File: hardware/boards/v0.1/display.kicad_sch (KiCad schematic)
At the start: 10 parts, among them U26 ER-TFT028A-4, U37 ER-TPC028-4.1

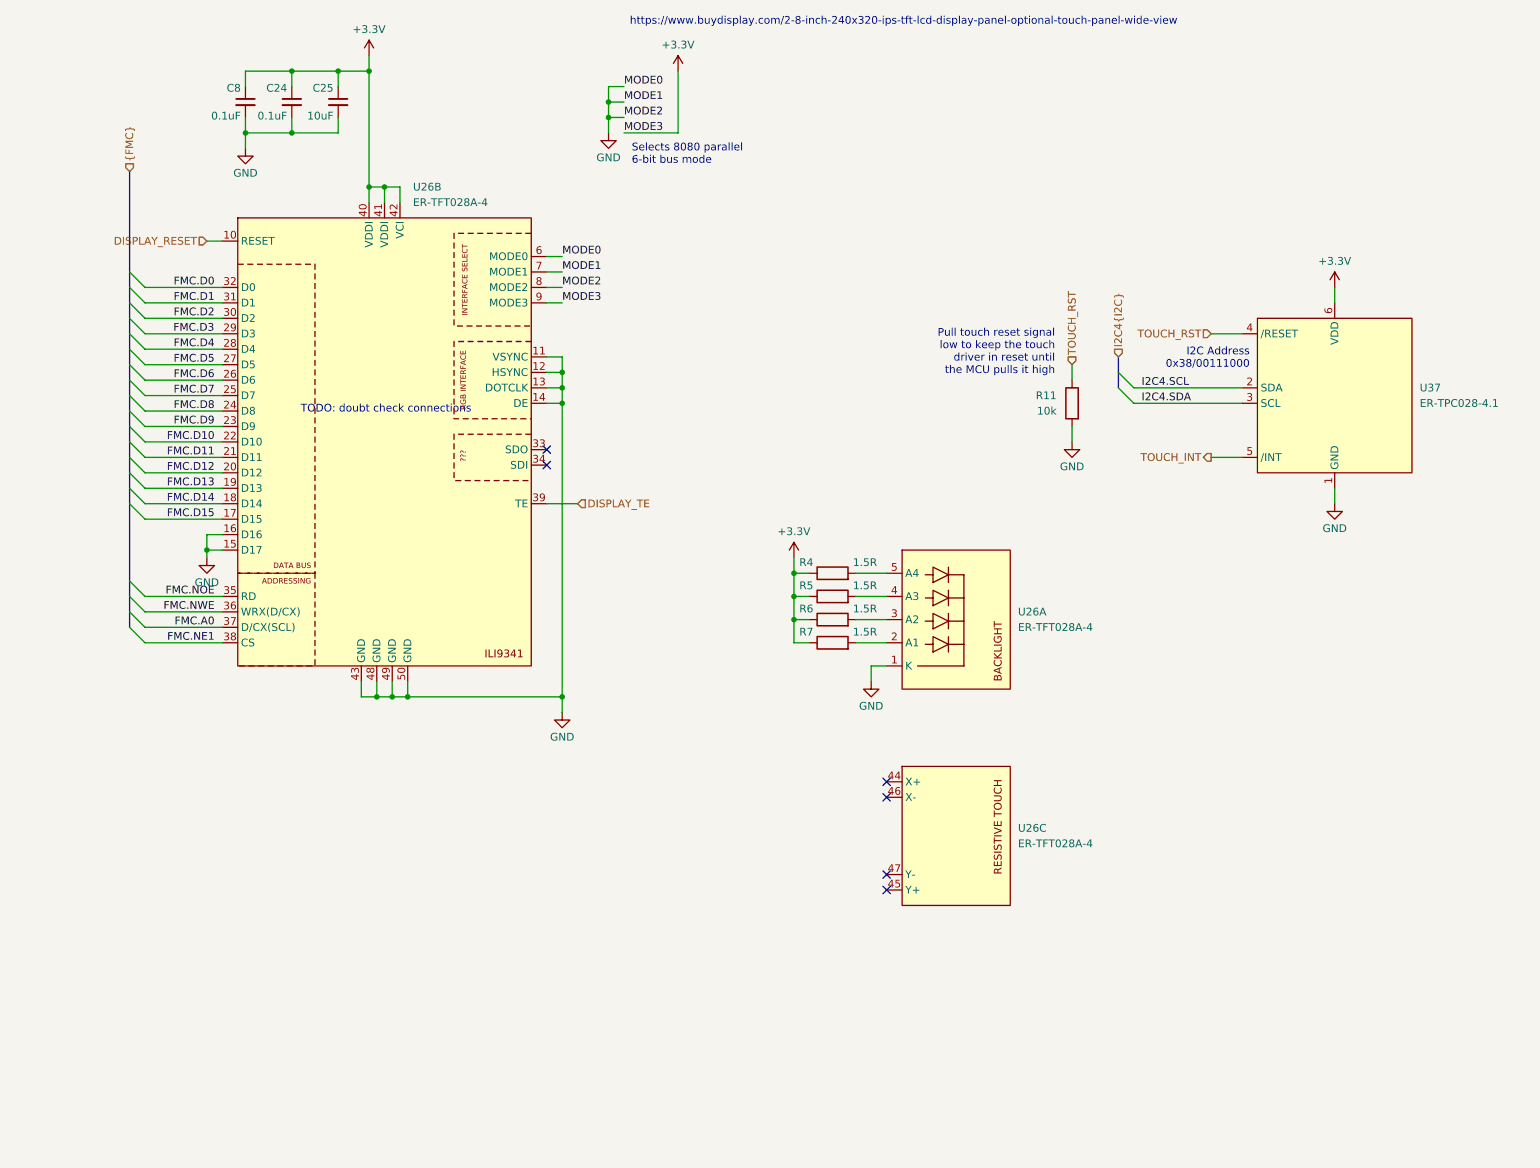
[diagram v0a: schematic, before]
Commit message: feat: routing cleanup and start of BOM selection
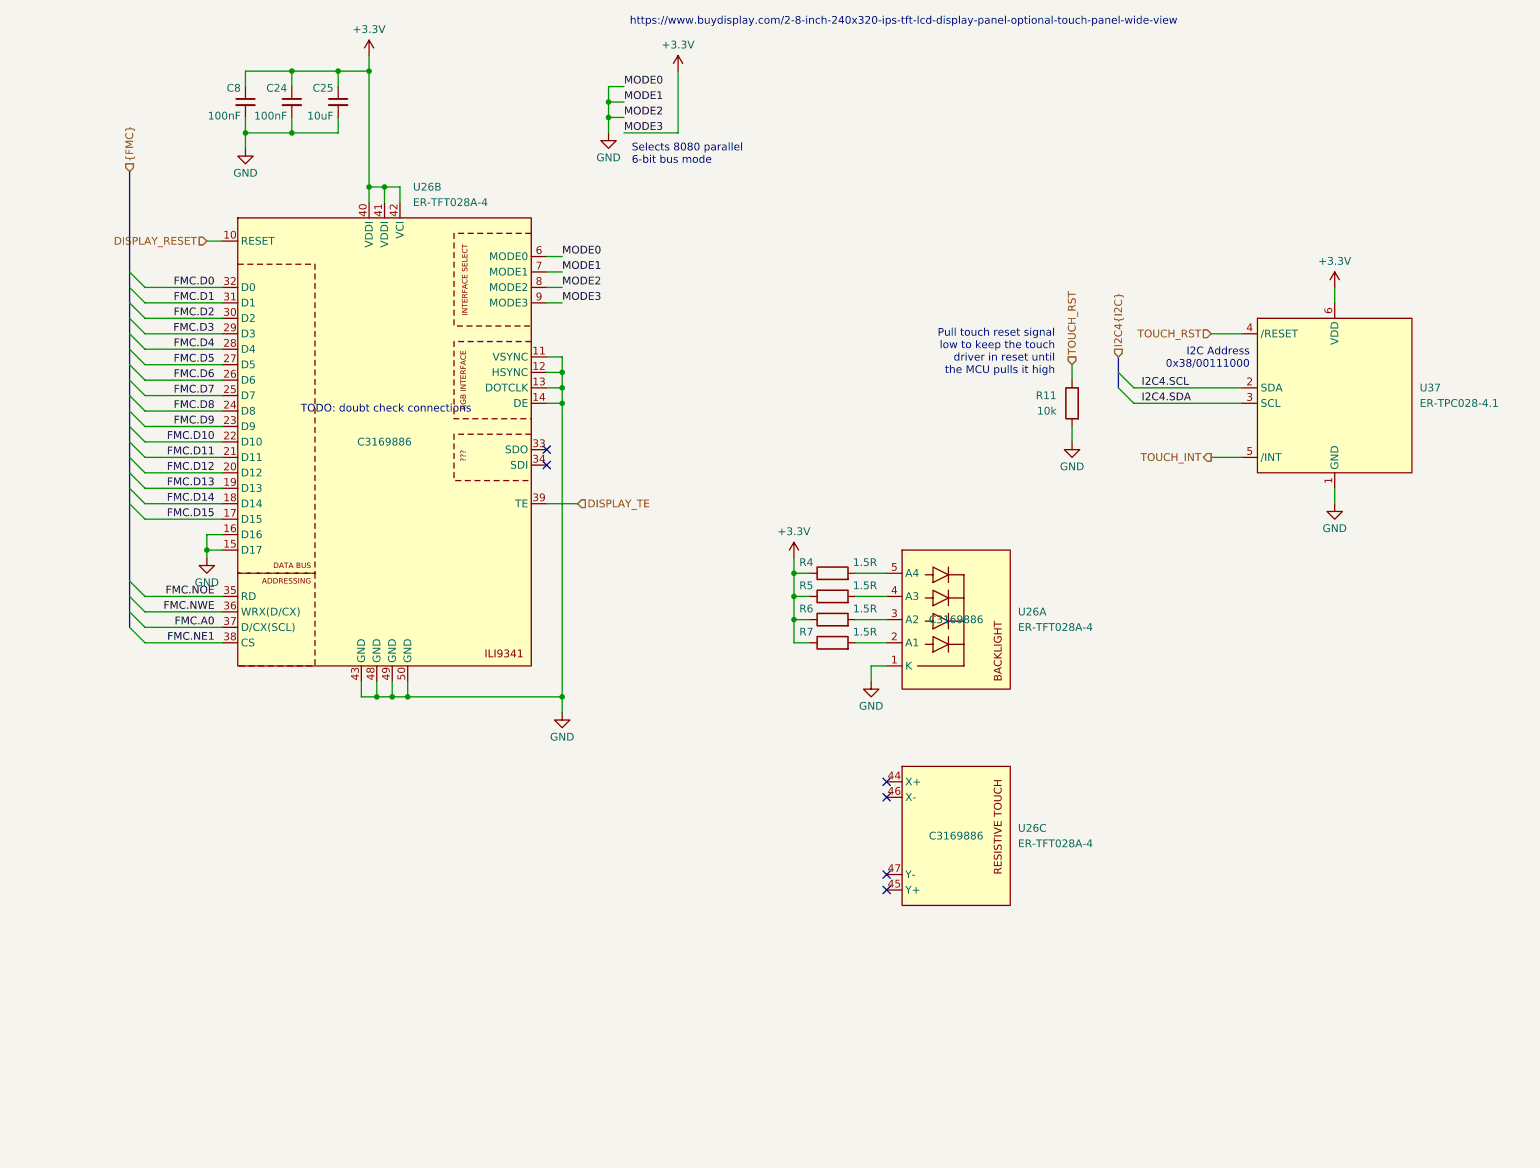
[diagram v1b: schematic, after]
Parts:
- C24, C8: value 0.1uF -> 100nF; JLC (none) -> C1525
- C25: JLC (none) -> C15525
- R11: JLC (none) -> C25531
- R4, R5, R6, R7: JLC (none) -> C100605
- U26: Connector (none) -> C3169886; JLC (none) -> C3169886
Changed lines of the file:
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@@
+			)
+		)
+		(property "JLC" "C100605"
+			(at 139.7 114.3 0)
+			(effects
+				(font
+					(size 1.27 1.27)
+				)
+				(hide yes)
 			)
 		)
@@
 			)
 		)
+		(property "JLC" "C100605"
+			(at 139.7 110.49 0)
+			(effects
+				(font
+					(size 1.27 1.27)
+				)
+				(hide yes)
+			)
+		)
 		(pin "2"
 		)
@@
 					(size 1.27 1.27)
 				)
+			)
+		)
+		(property "JLC" "C100605"
+			(at 139.7 118.11 0)
+			(effects
+				(font
+					(size 1.27 1.27)
+				)
+				(hide yes)
 			)
 		)
@@
 			)
 		)
+		(property "JLC" "C25531"
+			(at 179.07 82.55 0)
+			(effects
+				(font
+					(size 1.27 1.27)
+				)
+				(hide yes)
+			)
+		)
 		(pin "1"
 		)
@@
 					(size 1.27 1.27)
 				)
+			)
+		)
+		(property "JLC" "C15525"
+			(at 58.42 33.02 0)
+			(effects
+				(font
+					(size 1.27 1.27)
+				)
+				(hide yes)
 			)
 		)
@@
 			)
 		)
-		(property "Connector" ""
+		(property "Connector" "C3169886"
 			(at 160.02 153.67 0)
 			(effects
@@
 					(size 1.27 1.27)
 				)
+			)
+		)
+		(property "JLC" "C3169886"
+			(at 160.02 153.67 0)
+			(effects
+				(font
+					(size 1.27 1.27)
+				)
+				(hide yes)
 			)
 		)
@@
 			)
 		)
-		(property "Connector" ""
+		(property "Connector" "C3169886"
 			(at 66.04 88.9 0)
 			(effects
@@
 					(size 1.27 1.27)
 				)
+			)
+		)
+		(property "JLC" "C3169886"
+			(at 66.04 88.9 0)
+			(effects
+				(font
+					(size 1.27 1.27)
+				)
+				(hide yes)
 			)
 		)
@@
 					(size 1.27 1.27)
 				)
+			)
+		)
+		(property "JLC" "C100605"
+			(at 139.7 121.92 0)
+			(effects
+				(font
+					(size 1.27 1.27)
+				)
+				(hide yes)
 			)
 		)
@@
 			)
 		)
-		(property "Connector" ""
+		(property "Connector" "C3169886"
 			(at 160.02 118.11 0)
 			(effects
@@
 					(size 1.27 1.27)
 				)
+			)
+		)
+		(property "JLC" "C3169886"
+			(at 160.02 118.11 0)
+			(effects
+				(font
+					(size 1.27 1.27)
+				)
+				(hide yes)
 			)
 		)
@@
 			)
 		)
-		(property "Value" "0.1uF"
+		(property "Value" "100nF"
 			(at 50.038 35.306 0)
 			(effects
@@
 					(size 1.27 1.27)
 				)
+			)
+		)
+		(property "JLC" "C1525"
+			(at 50.8 33.02 0)
+			(effects
+				(font
+					(size 1.27 1.27)
+				)
+				(hide yes)
 			)
 		)
@@
 			)
 		)
-		(property "Value" "0.1uF"
+		(property "Value" "100nF"
 			(at 42.418 35.306 0)
 			(effects
@@
 			)
 		)
+		(property "JLC" "C1525"
+			(at 43.18 33.02 0)
+			(effects
+				(font
+					(size 1.27 1.27)
+				)
+				(hide yes)
+			)
+		)

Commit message: feat: various routing cleanup, add SD flash
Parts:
- U37: now left out of the parts list
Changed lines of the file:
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@@
+			)
+		)
+		(property "Part" ""
+			(at 139.7 114.3 0)
+			(effects
+				(font
+					(size 1.27 1.27)
+				)
 			)
 		)
@@
 			)
 		)
+		(property "Part" ""
+			(at 139.7 110.49 0)
+			(effects
+				(font
+					(size 1.27 1.27)
+				)
+			)
+		)
 		(pin "2"
 		)
@@
 				)
 				(hide yes)
+			)
+		)
+		(property "Part" ""
+			(at 139.7 118.11 0)
+			(effects
+				(font
+					(size 1.27 1.27)
+				)
 			)
 		)
@@
 			)
 		)
+		(property "Part" ""
+			(at 179.07 82.55 0)
+			(effects
+				(font
+					(size 1.27 1.27)
+				)
+			)
+		)
 		(pin "1"
 		)
@@
 				)
 				(hide yes)
+			)
+		)
+		(property "Part" ""
+			(at 58.42 33.02 0)
+			(effects
+				(font
+					(size 1.27 1.27)
+				)
 			)
 		)
@@
 			)
 		)
+		(property "Part" ""
+			(at 160.02 153.67 0)
+			(effects
+				(font
+					(size 1.27 1.27)
+				)
+			)
+		)
 		(pin "38"
 		)
@@
 			)
 		)
+		(property "Part" ""
+			(at 66.04 88.9 0)
+			(effects
+				(font
+					(size 1.27 1.27)
+				)
+			)
+		)
 		(pin "38"
 		)
@@
 				)
 				(hide yes)
+			)
+		)
+		(property "Part" ""
+			(at 139.7 121.92 0)
+			(effects
+				(font
+					(size 1.27 1.27)
+				)
 			)
 		)
@@
 			)
 		)
+		(property "Part" ""
+			(at 160.02 118.11 0)
+			(effects
+				(font
+					(size 1.27 1.27)
+				)
+			)
+		)
 		(pin "38"
 		)
@@
 			)
 		)
+		(property "Part" ""
+			(at 50.8 33.02 0)
+			(effects
+				(font
+					(size 1.27 1.27)
+				)
+			)
+		)
 		(pin "1"
 		)
@@
 			)
 		)
+		(property "Part" ""
+			(at 43.18 33.02 0)
+			(effects
+				(font
+					(size 1.27 1.27)
+				)
+			)
+		)
 		(pin "1"
 		)
@@
 		(unit 1)
 		(exclude_from_sim no)
-		(in_bom yes)
+		(in_bom no)
 		(on_board yes)
 		(dnp no)
@@
 			)
 		)
+		(property "Part" ""
+			(at 222.25 81.28 0)
+			(effects
+				(font
+					(size 1.27 1.27)
+				)
+			)
+		)

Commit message: feat: swap out of stock components
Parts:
- U26: now left out of the parts list
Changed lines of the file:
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@@
 		(unit 3)
 		(exclude_from_sim no)
-		(in_bom yes)
+		(in_bom no)
 		(on_board yes)
 		(dnp no)
@@
 		(unit 2)
 		(exclude_from_sim no)
-		(in_bom yes)
+		(in_bom no)
 		(on_board yes)
 		(dnp no)
@@
 		(unit 1)
 		(exclude_from_sim no)
-		(in_bom yes)
+		(in_bom no)
 		(on_board yes)
 		(dnp no)

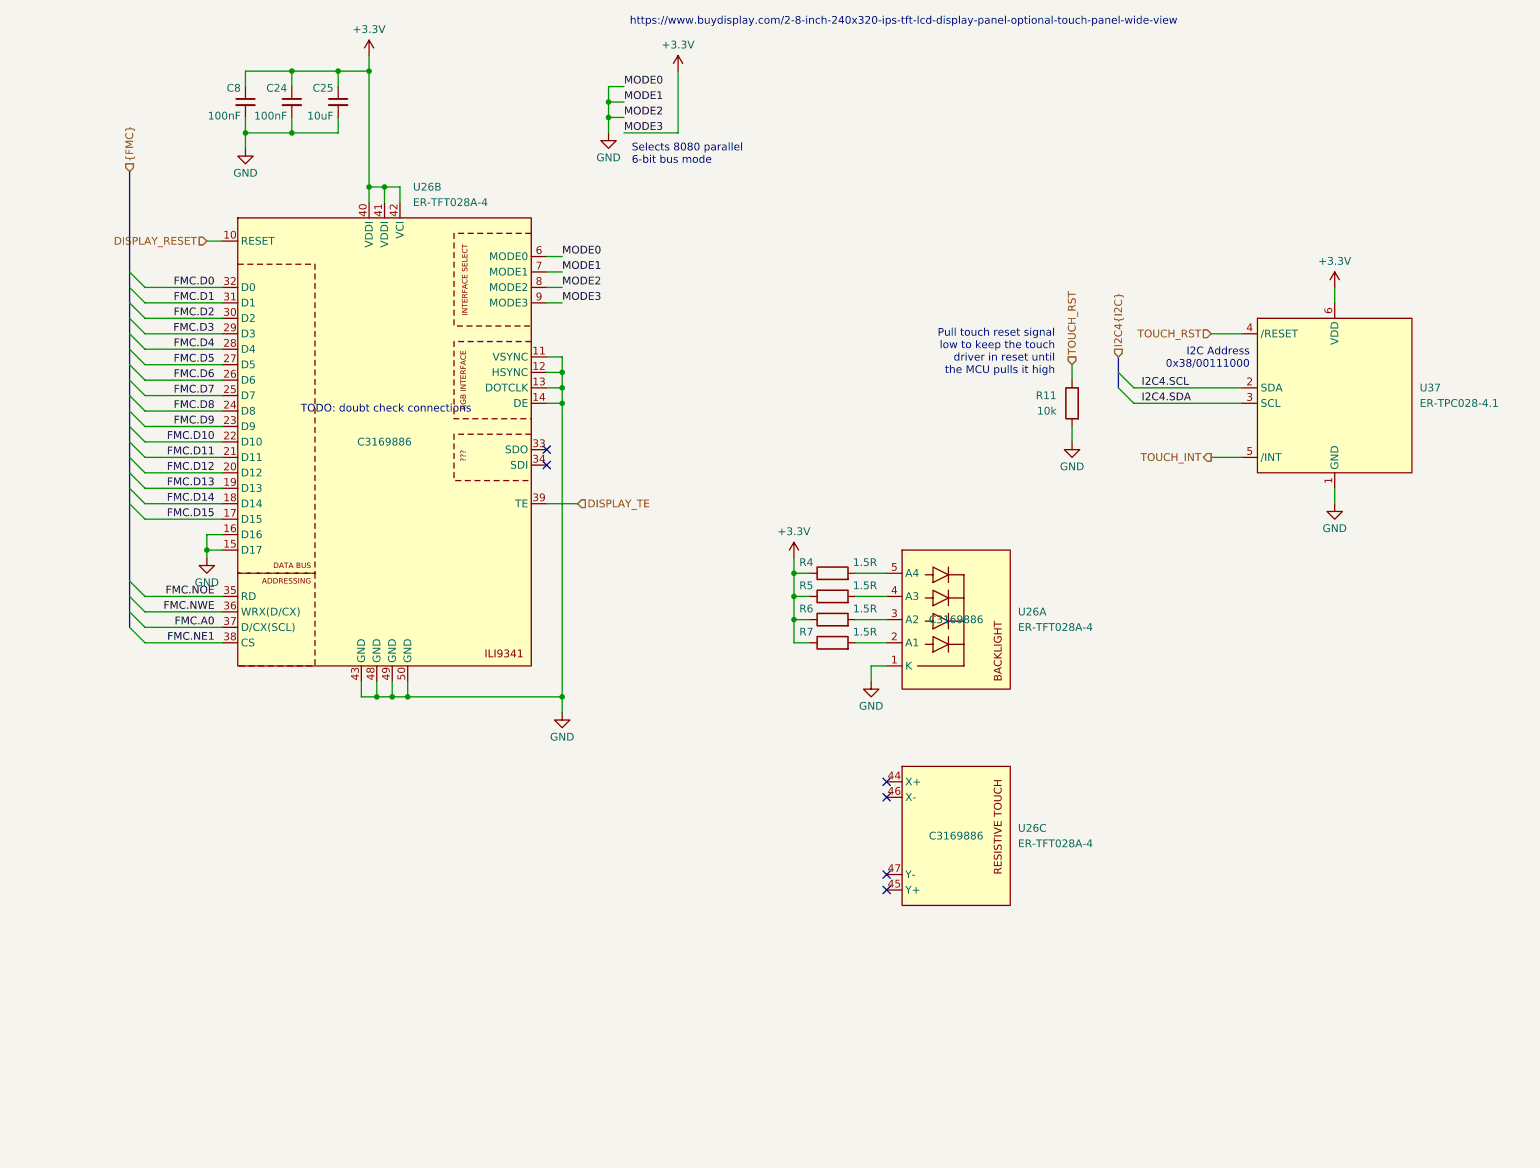
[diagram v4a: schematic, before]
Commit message: feat: various cleanup and BOM adjustment, split audio in into two switches
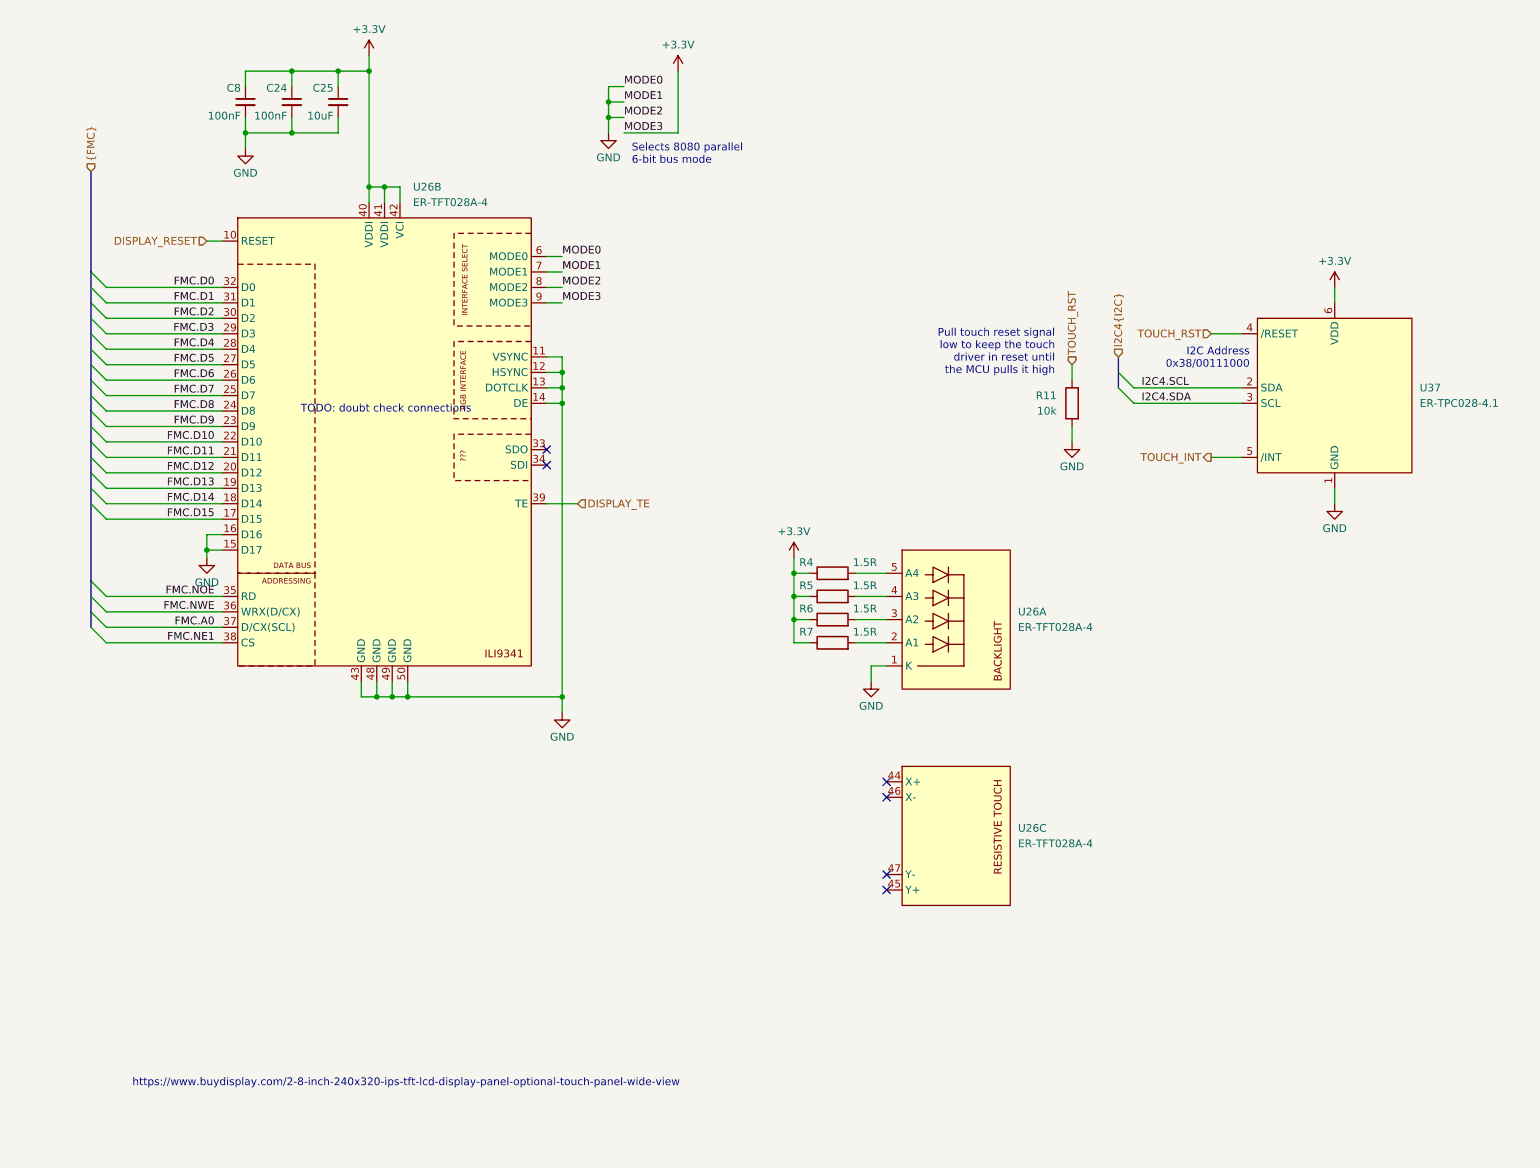
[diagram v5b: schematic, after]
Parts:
- U26: Connector C3169886 -> (none)
